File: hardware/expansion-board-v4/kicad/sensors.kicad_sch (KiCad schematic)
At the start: 30 parts, among them J2 U.FL_GNSS_EXT(经尾线转SMA), J8 U.FL→内置patch, Q4 AO3401A, Q5 AO3401A, U17 XA17-G4K(或AS179-92LF), U4 BNO085, U5 BMP388, U6 QMC5883P, U7 ATGM336H-6N-74

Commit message: fix(v4): correct GNSS antenna bias control
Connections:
- net ANT_SEL_GNSS_A: now also Q4.1 (G); no longer Q5.1 (G)
- net ANT_SEL_GNSS_B: now also Q5.1 (G); no longer Q4.1 (G)
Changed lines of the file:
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@@
 		)
 	)
-	(global_label "ANT_SEL_GNSS_B"
+	(global_label "ANT_SEL_GNSS_A"
 		(shape passive)
 		(at 274.32 88.9 180)
@@
 		)
 	)
-	(global_label "ANT_SEL_GNSS_A"
+	(global_label "ANT_SEL_GNSS_B"
 		(shape passive)
 		(at 274.32 114.3 180)

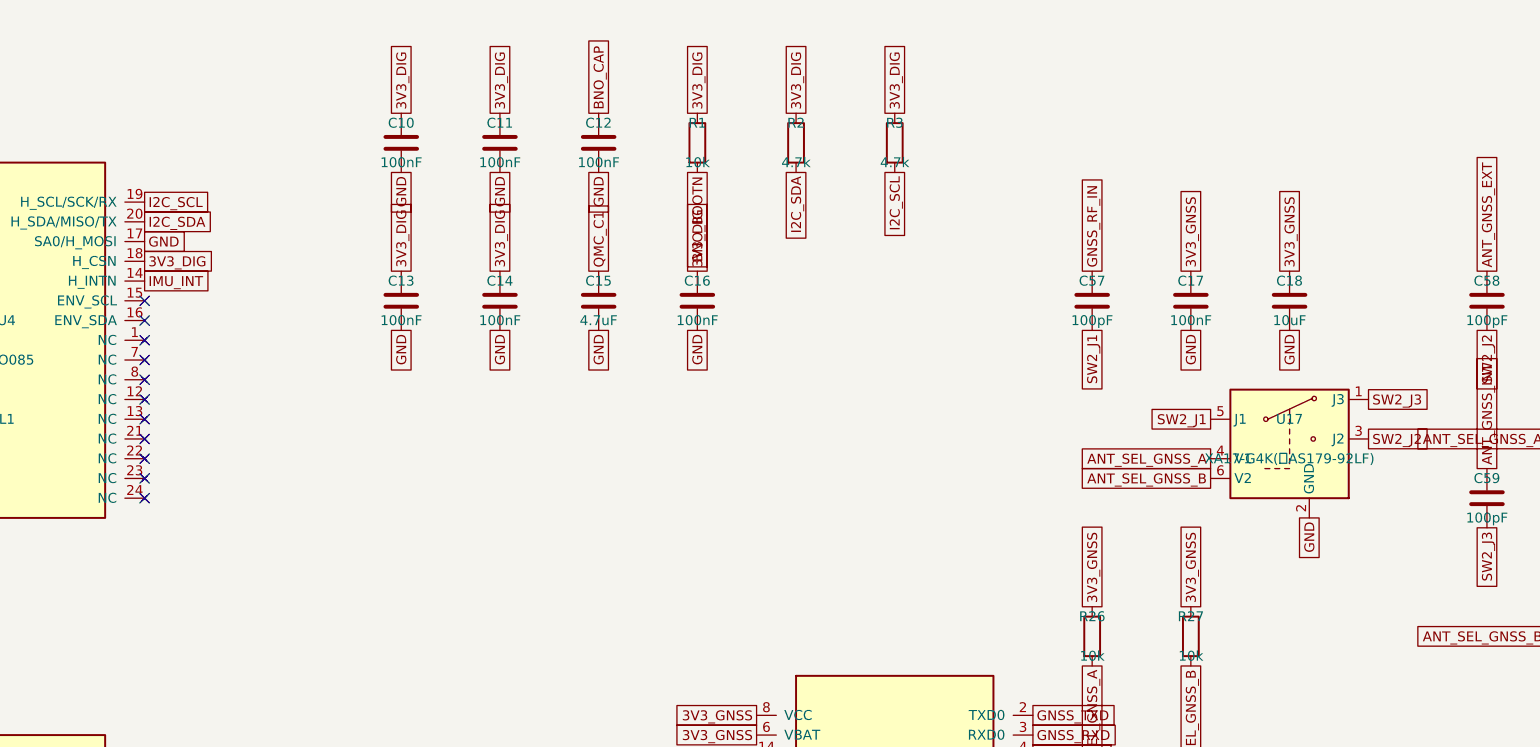
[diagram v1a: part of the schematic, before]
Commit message: fix(v4): finalize V4.3 board after manual routing
罩哥手工完成全部布线后的定稿。DRC 0 violations / 0 unconnected。

板子本身:
- 1607 段走线 / 415 个过孔 / 207 个封装 / 15 个 zone
- RP_1V1 在 B.Cu 合并为单块 228.96mm2，四颗 RP_1V1 去耦落入其中
- C81 挪到 U12 旁 1.47mm(原 3.36mm)，脚下由「无铜」变为落在 B.Cu 的 3V3_RF 上
- U8.23(DVDD) 补一个 RP_1V1 过孔 @(85.798,72.600)，接入距离 1.63 -> 0.88mm
  落点在既有走线上，未改任何走线；与相邻 QFN 焊盘边缘间距 +0.312mm

原理图:
- rf1090 的 PWR_FLAG 由 #FLG05 改为 #FLG06。sheet_power.py 已占用 #FLG05,
  两页撞号会让网表导出报「批注错误」。改后网表 714 节点、网络归属零变化。

.kicad_pro 保留正式板原有的 FINE netclass(0.13mm, 用于 DEMOD0-3/RECOVERED_CLK/
SWCLK/SWDIO)。板上这 7 个网络实际都按 0.15mm 布线、FINE 处于闲置; 两份工程
文件下各跑一次 DRC 均为 0，且 drc_exclusions 都是空的。
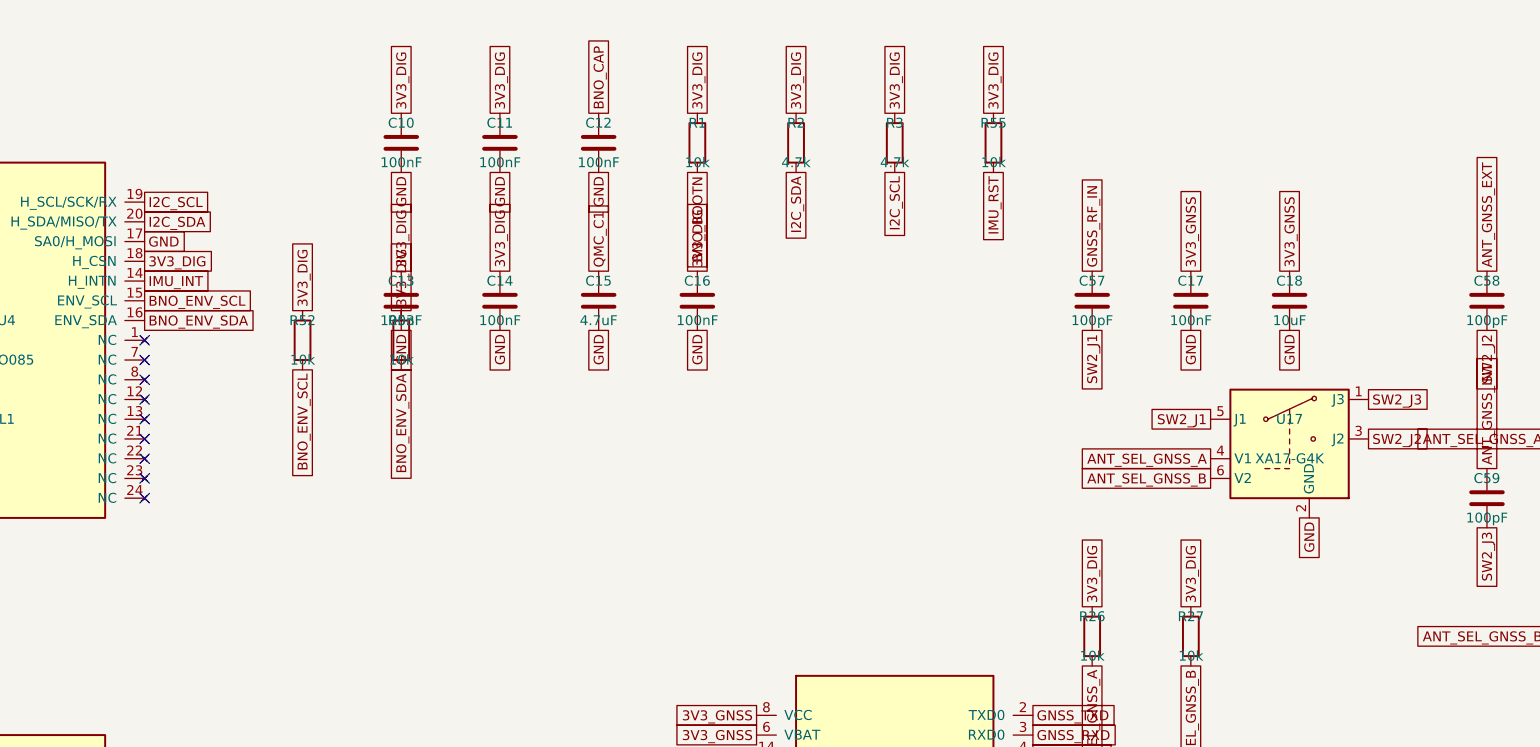
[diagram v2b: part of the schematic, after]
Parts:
- added R52, R53: 10k, Resistor_SMD:R_0402_1005Metric, symbol Device:R
- added R55: 10k, Resistor_SMD:R_0603_1608Metric, symbol Device:R
- U17: value XA17-G4K(或AS179-92LF) -> XA17-G4K
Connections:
- net 3V3_DIG: now also R26.1, R27.1, R52.1, R53.1, R55.1
- net 3V3_GNSS: no longer R26.1, R27.1
- net IMU_RST: now also R55.2
- net BNO_ENV_SCL: now reaches U4.15 (ENV_SCL)
- net BNO_ENV_SCL: now also R52.2
- net BNO_ENV_SDA: now reaches U4.16 (ENV_SDA)
- net BNO_ENV_SDA: now also R53.2
- no-connect marks 31 -> 29
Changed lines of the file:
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@@
 		(at 58.42 83.82)
 	)
+	(global_label "BNO_ENV_SCL"
+		(shape passive)
+		(at 93.98 71.12 0)
+		(effects (font (size 1.27 1.27)) (justify left))
+	)
+	(global_label "BNO_ENV_SDA"
+		(shape passive)
+		(at 93.98 73.66 0)
+		(effects (font (size 1.27 1.27)) (justify left))
+	)
 	(global_label "I2C_SCL"
 		(shape passive)
@@
 	)
 	(no_connect
-		(at 93.98 71.12)
-	)
-	(no_connect
-		(at 93.98 73.66)
-	)
-	(no_connect
 		(at 93.98 76.2)
 	)
@@
 	(no_connect
 		(at 93.98 96.52)
+	)
+	(symbol
+		(lib_id "Device:R")
+		(at 114.3 76.2 0)
+		(unit 1)
+		(exclude_from_sim no)
+		(in_bom yes)
+		(on_board yes)
+		(dnp no)
+		(property "Reference" "R52"
+			(at 114.3 73.66 0)
+			(effects (font (size 1.27 1.27)))
+		)
+		(property "Value" "10k"
+			(at 114.3 78.74 0)
+			(effects (font (size 1.27 1.27)))
+		)
+		(property "Footprint" "Resistor_SMD:R_0402_1005Metric"
+			(at 114.3 81.28 0)
+			(effects (font (size 1.27 1.27))
+				(hide yes))
+		)
+		(property "Datasheet" "~"
+			(at 114.3 83.82 0)
+			(effects (font (size 1.27 1.27))
+				(hide yes))
+		)
+		(pin "1"
+		)
+		(pin "2"
+		)
+		(instances
+			(project "expansion-board-v4"
+				(path "/10000000-0000-4000-8000-000000000001/20000000-0000-4000-8000-000000000005"
+					(reference "R52")
+					(unit 1)
+				)
+			)
+		)
+	)
+	(global_label "3V3_DIG"
+		(shape passive)
+		(at 114.3 72.39 270)
+		(effects (font (size 1.27 1.27)) (justify left))
+	)
+	(global_label "BNO_ENV_SCL"
+		(shape passive)
+		(at 114.3 80.01 90)
+		(effects (font (size 1.27 1.27)) (justify right))
+	)
+	(symbol
+		(lib_id "Device:R")
+		(at 127 76.2 0)
+		(unit 1)
+		(exclude_from_sim no)
+		(in_bom yes)
+		(on_board yes)
+		(dnp no)
+		(property "Reference" "R53"
+			(at 127 73.66 0)
+			(effects (font (size 1.27 1.27)))
+		)
+		(property "Value" "10k"
+			(at 127 78.74 0)
+			(effects (font (size 1.27 1.27)))
+		)
+		(property "Footprint" "Resistor_SMD:R_0402_1005Metric"
+			(at 127 81.28 0)
+			(effects (font (size 1.27 1.27))
+				(hide yes))
+		)
+		(property "Datasheet" "~"
+			(at 127 83.82 0)
+			(effects (font (size 1.27 1.27))
+				(hide yes))
+		)
+		(pin "1"
+		)
+		(pin "2"
+		)
+		(instances
+			(project "expansion-board-v4"
+				(path "/10000000-0000-4000-8000-000000000001/20000000-0000-4000-8000-000000000005"
+					(reference "R53")
+					(unit 1)
+				)
+			)
+		)
+	)
+	(global_label "3V3_DIG"
+		(shape passive)
+		(at 127 72.39 270)
+		(effects (font (size 1.27 1.27)) (justify left))
+	)
+	(global_label "BNO_ENV_SDA"
+		(shape passive)
+		(at 127 80.01 90)
+		(effects (font (size 1.27 1.27)) (justify right))
 	)
 	(symbol
@@
 	(symbol
 		(lib_id "Device:R")
+		(at 203.2 50.8 0)
+		(unit 1)
+		(exclude_from_sim no)
+		(in_bom yes)
+		(on_board yes)
+		(dnp no)
+		(property "Reference" "R55"
+			(at 203.2 48.26 0)
+			(effects (font (size 1.27 1.27)))
+		)
+		(property "Value" "10k"
+			(at 203.2 53.34 0)
+			(effects (font (size 1.27 1.27)))
+		)
+		(property "Footprint" "Resistor_SMD:R_0603_1608Metric"
+			(at 203.2 55.88 0)
+			(effects (font (size 1.27 1.27))
+				(hide yes))
+		)
+		(property "Datasheet" "~"
+			(at 203.2 58.42 0)
+			(effects (font (size 1.27 1.27))
+				(hide yes))
+		)
+		(pin "1"
+		)
+		(pin "2"
+		)
+		(instances
+			(project "expansion-board-v4"
+				(path "/10000000-0000-4000-8000-000000000001/20000000-0000-4000-8000-000000000005"
+					(reference "R55")
+					(unit 1)
+				)
+			)
+		)
+	)
+	(global_label "3V3_DIG"
+		(shape passive)
+		(at 203.2 46.99 270)
+		(effects (font (size 1.27 1.27)) (justify left))
+	)
+	(global_label "IMU_RST"
+		(shape passive)
+		(at 203.2 54.61 90)
+		(effects (font (size 1.27 1.27)) (justify right))
+	)
+	(symbol
+		(lib_id "Device:R")
 		(at 177.8 50.8 0)
 		(unit 1)
@@
 			(effects (font (size 1.27 1.27)))
 		)
-		(property "Value" "XA17-G4K(或AS179-92LF)"
+		(property "Value" "XA17-G4K"
 			(at 241.3 91.44 0)
 			(effects (font (size 1.27 1.27)))
@@
 		)
 	)
-	(global_label "3V3_GNSS"
+	(global_label "3V3_DIG"
 		(shape passive)
 		(at 215.9 110.49 270)
@@
 		)
 	)
-	(global_label "3V3_GNSS"
+	(global_label "3V3_DIG"
 		(shape passive)
 		(at 228.6 110.49 270)

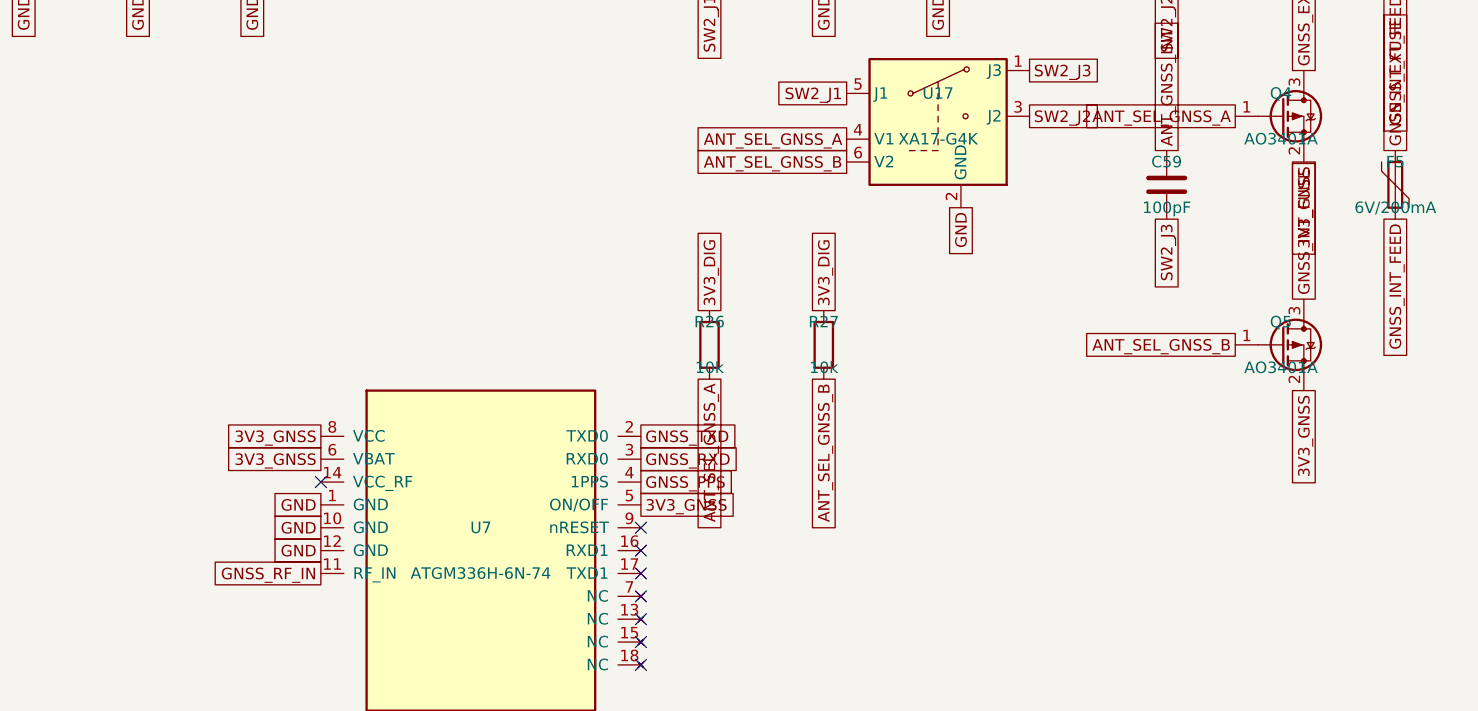
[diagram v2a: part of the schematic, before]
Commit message: hardware: v4 走线固化 + V4.5 发布包 + 装配站点/子项目
- v3/v4 kicad_pcb 重新布线; export_routes 快照 ROUTES.json(1609 段/438 孔)。
- V4.5 Gerber/KiCad 发布包(20260911); cal-board/fpc-antenna 子项目;
  web/assembly 装配站点与生成工具; V4.6 airband BOM 草案。
- 文档: BASEBOARD_REF / ASSEMBLY / SELECTIVE_PLACEMENT 等同步。
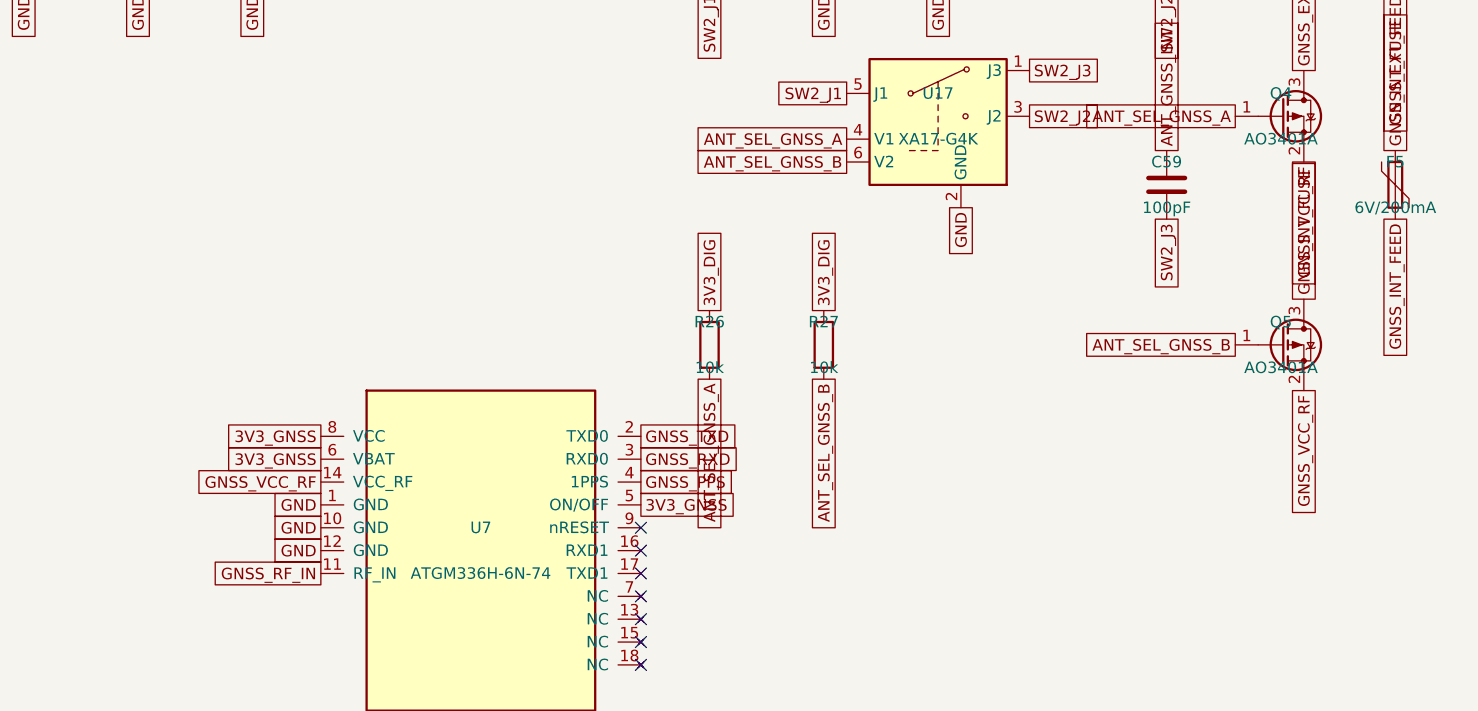
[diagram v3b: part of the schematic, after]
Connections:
- net 3V3_GNSS: no longer Q4.2 (S), Q5.2 (S)
- net GNSS_VCC_RF: now reaches U7.14 (VCC_RF)
- net GNSS_VCC_RF: now also Q4.2 (S), Q5.2 (S)
- no-connect marks 29 -> 28
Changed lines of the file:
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@@
 		(effects (font (size 1.27 1.27)) (justify right))
 	)
-	(no_connect
-		(at 172.72 129.54)
+	(global_label "GNSS_VCC_RF"
+		(shape passive)
+		(at 172.72 129.54 180)
+		(effects (font (size 1.27 1.27)) (justify right))
 	)
 	(global_label "GNSS_RF_IN"
@@
 		(effects (font (size 1.27 1.27)) (justify right))
 	)
-	(global_label "3V3_GNSS"
+	(global_label "GNSS_VCC_RF"
 		(shape passive)
 		(at 281.94 93.98 90)
@@
 		(effects (font (size 1.27 1.27)) (justify right))
 	)
-	(global_label "3V3_GNSS"
+	(global_label "GNSS_VCC_RF"
 		(shape passive)
 		(at 281.94 119.38 90)

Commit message: hardware(v4.7): 修正 C99 并刷新整套制造与装配文件
在用户修订的布局上将 C99 改为 100nF/0402，复用 C37/C52 的 C307331；同步原理图版本、BOM/CPL、装配图、安装助手及制造归档，更新下单入口和未决电气项。

验证：DRC 0 违规/0 未连通，存盘覆铜与包源一致性已核对；提交前版本包/安装助手20项，18通过、2跳过。元件契约中已记录的 C84 两条子断言失败按用户范围保留；Y4 供电和 U22 VREF 建议尚待闭环。内部工具、审计报告和采购过程文件按仓库规则仅留本地。
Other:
- title: Expansion Board V1 - Sensors + GNSS -> Expansion Board V4.7 - Sensors + GNSS
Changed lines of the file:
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@@
 	(paper "A3")
 	(title_block
-		(title "Expansion Board V1 - Sensors + GNSS")
+		(title "Expansion Board V4.7 - Sensors + GNSS")
 		(date "2026-08-01")
-		(rev "V1")
+		(rev "V4.7")
 		(company "Pilot Kit")
 	)

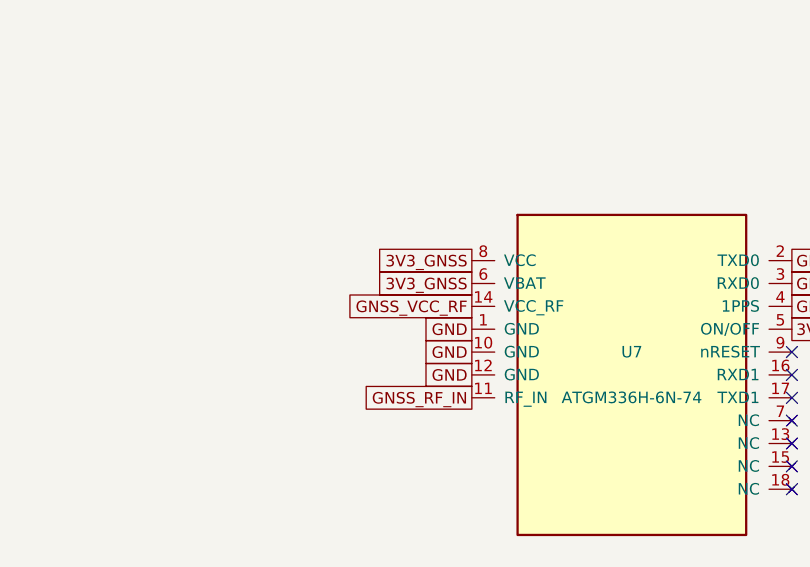
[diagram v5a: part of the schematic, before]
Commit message: hardware(v4.8): GNSS 模块 VBAT 常供电，开机不再冷启动
板上那颗 ATGM336H 本身就有 RTC（6N 手册 §2.4：pin6 VBAT = "RTC 及 SRAM 后备
电源"），但 pin6 一直接在 3V3_GNSS 上——与模块主供电同一条轨，关机
(BATFET_DIS) 时一起断电。于是模块每次开机都从零冷启动：既没有时间，也没有
星历。这同时是「开机没有时间」的硬件根因，和 gps_task.c 里 "gps-coarse" 粗校
兜底一直走不到的原因。

方案成立的前提先做了实机验证：室外定位后拔掉天线，让模块彻底失锁
(fix=0 sats=0 snr=0)，RMC 的时间字段仍逐秒前进 —— 模块的 RTC 确实独立于定位
在走。所以不需要外挂 RTC 芯片，板上已经有一颗，缺的只是一路不断电的 VBAT。

电路（6 件，取电点是 BAT_P：关机断的是 BAT→SYS，BAT_P 这侧照常带电）
    BAT_P ─[U23 TPS7A2033]─ 3V3_BKP ─[D7]─┬─ GNSS_VBAT ─ U7.pin6
                                          └─[R63 2.2k]─ BT1(+)
    C101/C102 = U23 的输入/输出去耦

  · U23 复用已采购料号 C2862740（BOM 用量 2→3），IGND 典型 6.5µA；
    加 GNSS 的 Ibat 10µA，总账约 17µA —— 对 5000mAh 是 33 年量级
  · D7 不能省：TPS7A20 手册写明输入掉电时电流会从 OUT 倒灌回 IN 并可能损坏
    器件。主电池被保护板切断后 BAT_P=0，没有它电池就会经 LDO 往回灌
  · BT1 = Seiko MS621FE-FL11E 焊接式可充电锂锰，5.5mAh，充到 2.91V 约 75%
    → 续航约 17 天。⚠️ 只能用 ML/MS 体系，**LIR 系列满电 4.2V 会超 Vbat 极限 3.6V**
  · 中途曾设计成「带线 CR2032 + 座子」（先 PH2.0 后 SH1.0），焊接式把座子和
    一颗 OR-ing 二极管一起省掉，"4.2V 主电池插错备份口"这条失效路径也随之消失

自建封装与 3D 模型（KiCad 官方库那个用不了）
  官方库有同名的 BatteryHolder_Seiko_MS621F，但它焊盘中心距 1.5mm，而
  FL11E 实际是 2.5mm，差 1mm 焊不上 —— 同一颗电池不同端子后缀
  （FL11E / FL01E / FE11E）焊脚并不通用，跟 J9 栽的是同一类坑。
  封装按 SII 官方样本 MicroBattery_E_20230330_rev05 第 14 页 1:1 建立。
  .wrl 里的圆柱必须用 IndexedFaceSet 显式建面：用 VRML 的 Cylinder 图元时
  整个元件都不显示（连焊脚的 Box 一起没），KiCad 静默忽略、不报错。

两个 DRC 抓不到的坑
  1) U7.pin6 改网络时必须连旧走线一起摘。焊盘改了网络而压在它上面的 4 段
     3V3_GNSS 铜不动，两个网络就被直接短在一起、二极管被旁路，而 DRC 只会
     报"未连通"不会报"短路"——它们确实是连着的。
  2) BT1 初版摆在 (142,107)，与 M2.5 安装孔 H4 实际重叠 2.39mm，DRC 全程
     0 违例：孔挂 F 面、电池在 B 面，按层查 courtyard 两边各自合规，但螺丝
     是贯穿的。重新求解时把四个贯穿孔一并当障碍，现落点 (140,76.4)，
     距投影区 +4.10 / 距板右边 +4.60 / 最近障碍 +14.26。

布线由用户手工完成并 review 通过：缺线 0 / 孤立断头铜 0 / 焊盘未接覆铜 0 /
铜层 DRC 0 / 丝印 DRC 0 / In1 参考面完整。BKP_CELL 走线 0.15mm 宽、68.9mm 长，
按 IPC-2221 载流约 0.6A 而实际电流 0.4mA，线阻 0.23Ω 相对串联的 R63=2.2k
占 0.01% —— 线宽不是约束，这条路的限流本来就由 R63 决定。

动了三处门禁（都说明理由）
  · test_board_revision_contract: 目标版本 V4.7 → V4.8（版本跟随）
  · test_v4_placement_contract / test_component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
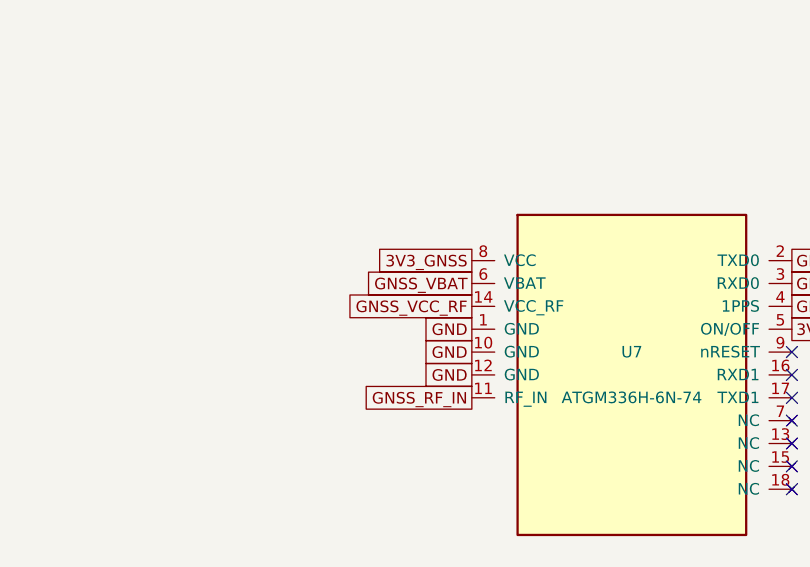
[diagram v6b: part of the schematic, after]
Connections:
- net 3V3_GNSS: no longer U7.6 (VBAT)
- new net GNSS_VBAT: U7.6 (VBAT)
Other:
- title: Expansion Board V4.7 - Sensors + GNSS -> Expansion Board V4.8 - Sensors + GNSS
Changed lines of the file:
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@@
 	(paper "A3")
 	(title_block
-		(title "Expansion Board V4.7 - Sensors + GNSS")
+		(title "Expansion Board V4.8 - Sensors + GNSS")
 		(date "2026-08-01")
-		(rev "V4.7")
+		(rev "V4.8")
 		(company "Pilot Kit")
 	)
@@
 		(effects (font (size 1.27 1.27)) (justify right))
 	)
-	(global_label "3V3_GNSS"
+	(global_label "GNSS_VBAT"
 		(shape passive)
 		(at 172.72 127 180)

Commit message: feat(v4.11): 固化扩展板并修正电池补偿
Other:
- title: Expansion Board V4.8 - Sensors + GNSS -> Expansion Board V4.11 - Sensors + GNSS
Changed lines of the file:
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@@
 	(paper "A3")
 	(title_block
-		(title "Expansion Board V4.8 - Sensors + GNSS")
+		(title "Expansion Board V4.11 - Sensors + GNSS")
 		(date "2026-08-01")
-		(rev "V4.8")
+		(rev "V4.11")
 		(company "Pilot Kit")
 	)
